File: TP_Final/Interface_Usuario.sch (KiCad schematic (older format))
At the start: 31 parts, among them J108 BG2, Q105 2N3904, Q106 2N3904, Q107 2N3904, SW102 KSR, SW103 KSR, SW104 KSR, SW105 KSR

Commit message: se agregan descripciones a componentes del esquemático
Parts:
- removed SW102, SW103, SW104, SW105: KSR, Button_Switch_THT:Push_E-Switch_KS01Q01, symbol Switch:SW_Push
- added SW102, SW103, SW104, SW105: KS01-B, Button_Switch_THT:Push_E-Switch_KS01Q01, symbol Switch:SW_MEC_5E
- BZ101: Description (none) -> Buzzer 12mm con oscilador de 5V; Manufac. (none) -> Loudity
- D105: Description (none) -> hree-lead bicolor T-1 3/4 (5mm) lamp witha central common a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; Manufac. (none) -> Fairchild
- DS101: Controlador (none) -> ILI9486; Descripción (none) -> Display TFT de 3.5\", conector compatible Arduino UNO, cont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; Fabricante (none) -> mcufriend; Part # (none) -> N/A
- J108: Description (none) -> Bloque de terminales de tornillo PCB; Manufac. (none) -> XINYA
- renumbered R112 to R111, R111 to R112
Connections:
- net GNDD: now also SW102.3 (K), SW102.4 (A), SW103.3 (K), SW103.4 (A), SW104.3 (K), SW104.4 (A), SW105.3 (K), SW105.4 (A)
- net LED_ROJO: now also R112.2; no longer R114.2
- net LED_VERDE: now also R114.2; no longer R112.2
- net at C118.1, R116.1: now also SW102.1, SW102.2
- net at C119.1, R117.1: now also SW103.1, SW103.2
- net at C121.1, R120.1: now also SW104.1, SW104.2
- net at C122.1, R121.1: now also SW105.1, SW105.2
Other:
- note added: "Display TFT de 3.5" con conector \ncompatible con Arduino UNO y \ncontrolador tipo ILI9486"
- moved on the sheet: C116, C117, D105, DS101, JP101, JP102, Q105, Q106, R111, R112, R113, R114

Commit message: Se avanza con el ruteo del PCB
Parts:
- Q106: footprint Package_TO_SOT_THT:TO-92L_HandSolder -> Package_TO_SOT_THT:TO-92_HandSolder
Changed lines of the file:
@@
 F 0 "Q106" H 8550 2225 50  0000 L CNN
 F 1 "2N3904" H 8550 2125 50  0000 L CNN
-F 2 "Package_TO_SOT_THT:TO-92L_HandSolder" H 9050 2300 50  0001 L CIN
+F 2 "Package_TO_SOT_THT:TO-92_HandSolder" H 9050 2300 50  0001 L CIN
 F 3 "https://www.onsemi.com/pub/Collateral/2N3903-D.PDF" H 8850 2375 50  0001 L CNN
 F 4 "TR170340" H 8850 2375 50  0001 C CNN "Elemon part"

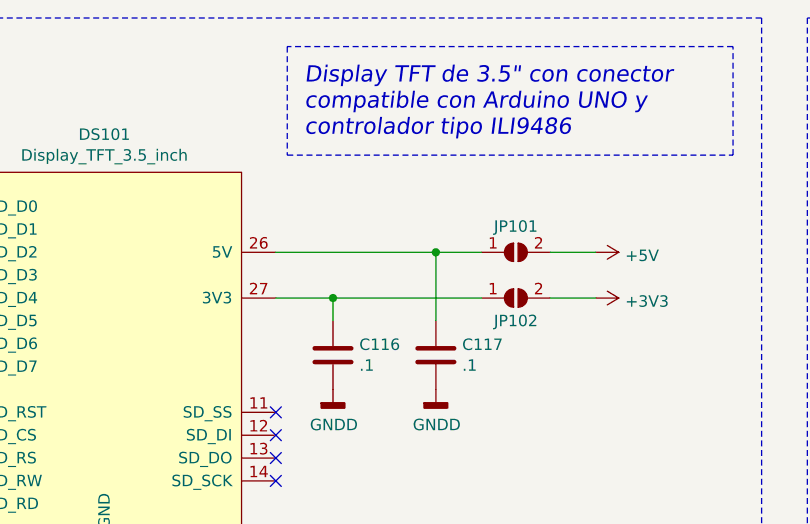
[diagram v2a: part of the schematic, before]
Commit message: Agrego agujeros de montaje y fiduciales al esquematico
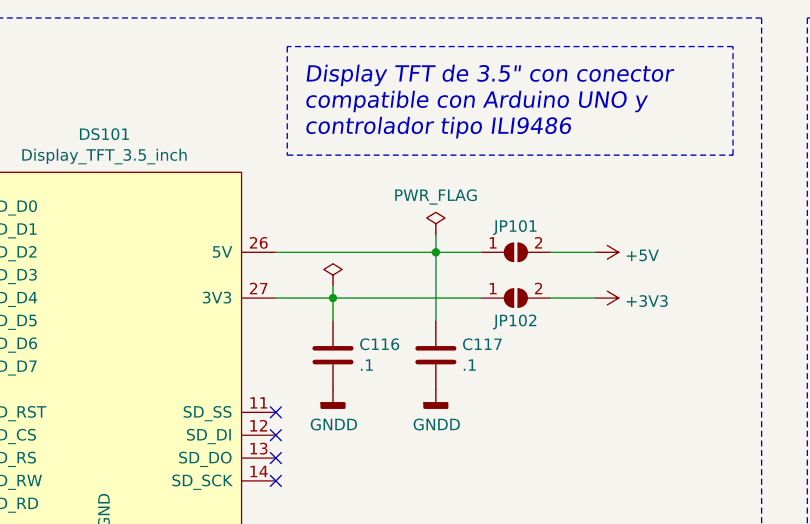
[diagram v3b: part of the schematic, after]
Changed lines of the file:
@@
 	1    0    0    -1
 $EndComp
+$Comp
+L power:PWR_FLAG #FLG0105
+U 1 1 607D479A
+P 5775 1500
+F 0 "#FLG0105" H 5775 1575 50  0001 C CNN
+F 1 "PWR_FLAG" H 5775 1673 50  0000 C CNN
+F 2 "" H 5775 1500 50  0001 C CNN
+F 3 "~" H 5775 1500 50  0001 C CNN
+	1    5775 1500
+	1    0    0    -1
+$EndComp
+$Comp
+L power:PWR_FLAG #FLG0106
+U 1 1 607D535B
+P 5325 1725
+F 0 "#FLG0106" H 5325 1800 50  0001 C CNN
+F 1 "PWR_FLAG" H 5325 1975 50  0001 C CNN
+F 2 "" H 5325 1725 50  0001 C CNN
+F 3 "~" H 5325 1725 50  0001 C CNN
+	1    5325 1725
+	1    0    0    -1
+$EndComp
+Wire Wire Line
+	5325 1725 5325 1775
+Wire Wire Line
+	5775 1500 5775 1575
 $EndSCHEMATC

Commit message: Se finaliza el diseño del PCB
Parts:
- BZ101: footprint Buzzer_Beeper:Buzzer_TDK_PS1240P02BT_D12.2mm_H6.5mm -> Buzzer_Beeper:Buzzer_12x9.5RM7.6
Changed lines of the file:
@@
 F 0 "BZ101" H 9250 3950 50  0000 C CNN
 F 1 "Buzzer" H 9250 3850 50  0000 C CNN
-F 2 "Buzzer_Beeper:Buzzer_TDK_PS1240P02BT_D12.2mm_H6.5mm" V 9025 3750 50  0001 C CNN
+F 2 "Buzzer_Beeper:Buzzer_12x9.5RM7.6" V 9025 3750 50  0001 C CNN
 F 3 "https://www.tme.eu/Document/e98051deb5318767fbb4534d8e5fd23c/ld-bzeg-1205.pdf" V 9025 3750 50  0001 C CNN
 F 4 "Loudity" H 9050 3650 50  0001 C CNN "Manufac."
